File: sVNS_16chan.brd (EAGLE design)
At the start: 56.9 x 26.4 mm, 56 parts, among them IC2 OPA990IDCKR, IC3 EFM8SB10F2G-A-QFN20, J1 M50-3631042, J2 M50-3631042, J3 M50-3631042, U1 NT3H2211W0FHKH, U2 LT8410EDC-1#TRMPBF, U3 MUX36S16IRSNR, U4 MUX36S16IRSNR

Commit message: Checkpoint 5. Closer to success?
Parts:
- moved R17 7.02 mm to (2.03, 10.7)
- moved R24 4.50 mm to (12.0, 20.0), turned to 270 degrees
- moved R27 2.32 mm to (1.52, 4.88)
- moved R12 1.83 mm to (14.1, 19.2)
- moved C14 1.36 mm to (3.96, 23.7)
- moved C3 1.22 mm to (4.65, 15.8)
- moved L1 0.36 mm to (6.68, 17.2), turned to 90 degrees
- moved R26 0.20 mm to (1.12, 8.64), turned to 180 degrees
- moved R23 0.15 mm to (9.35, 21.2), turned to 180 degrees
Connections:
- net +3.3V: now also R23.1; no longer L1.P$1, R23.2, U2.2
- net +3.3V_LT8410_VCC: now also L1.P$1, R23.2, U2.2; no longer R23.1
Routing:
- net +20V: track 0.27 -> 29.0 mm, vias 0 -> 5
- net GND: track 31.6 -> 45.2 mm, vias 2 -> 13
- net +20V_PIN: track 1.63 -> 12.4 mm
- net +3.3V: track 9.32 -> 18.1 mm, vias 0 -> 4
- net +3.3V_LT8410_VCC: track 2.75 -> 10.5 mm
- net I_OUT+: track 33.5 -> 40.4 mm, vias 3 -> 5
- net MUX36D08_+20V: track 1.71 -> 7.85 mm
- net MUX36S16B_+20V: track 0.00 -> 4.85 mm
- net OPAMP_+20V: track 1.62 -> 5.43 mm
- net MUX36S16A+20V: track 0.00 -> 3.44 mm
- net RSTB_/_C2CK: track 18.1 -> 21.2 mm
- net +3.3V_VDD: track 6.31 -> 9.28 mm
- net P2.7_/_C2D: track 13.5 -> 15.4 mm
- net SW: track 1.69 -> 3.17 mm
- net P0.5_SHDN: track 36.6 -> 36.0 mm
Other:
- board text added: "Converted 20V"
- board text added: "Generated 3.3V"

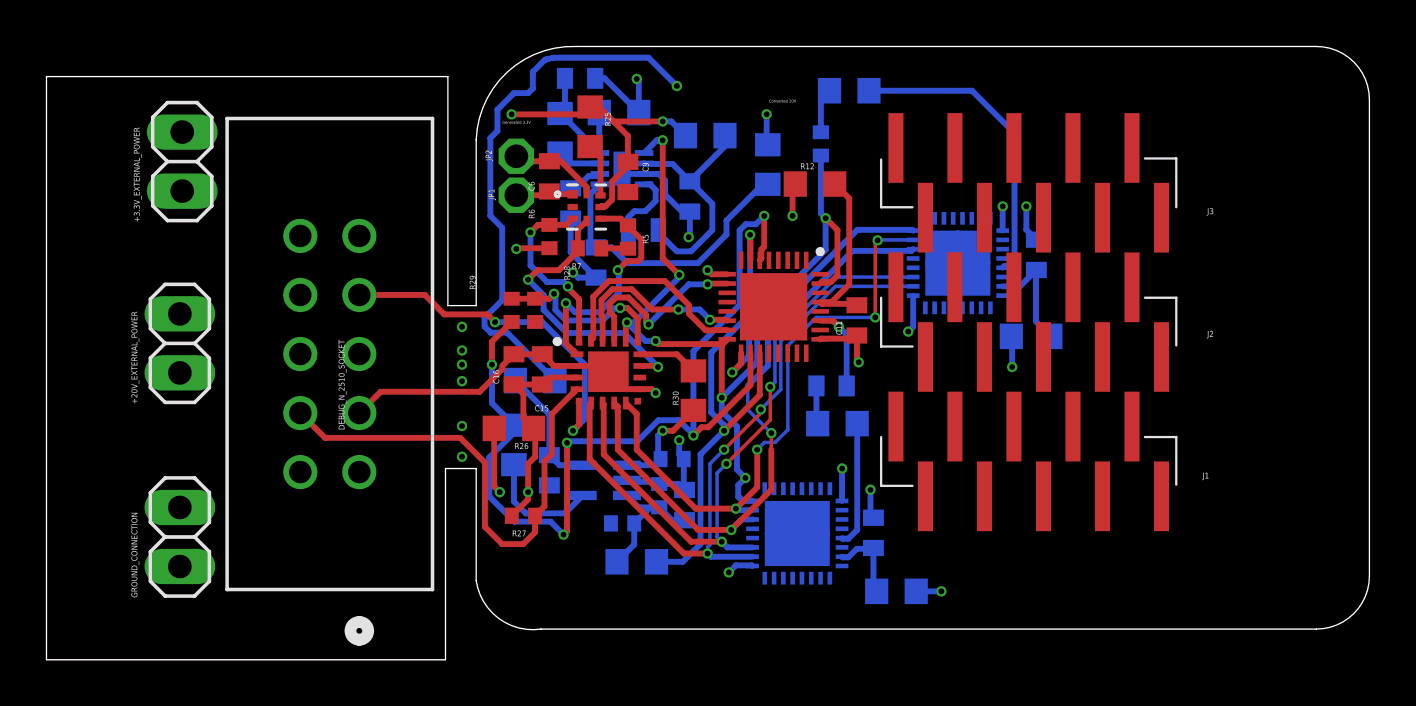
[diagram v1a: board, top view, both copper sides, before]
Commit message: Component routing finished. ready for output stage routing.
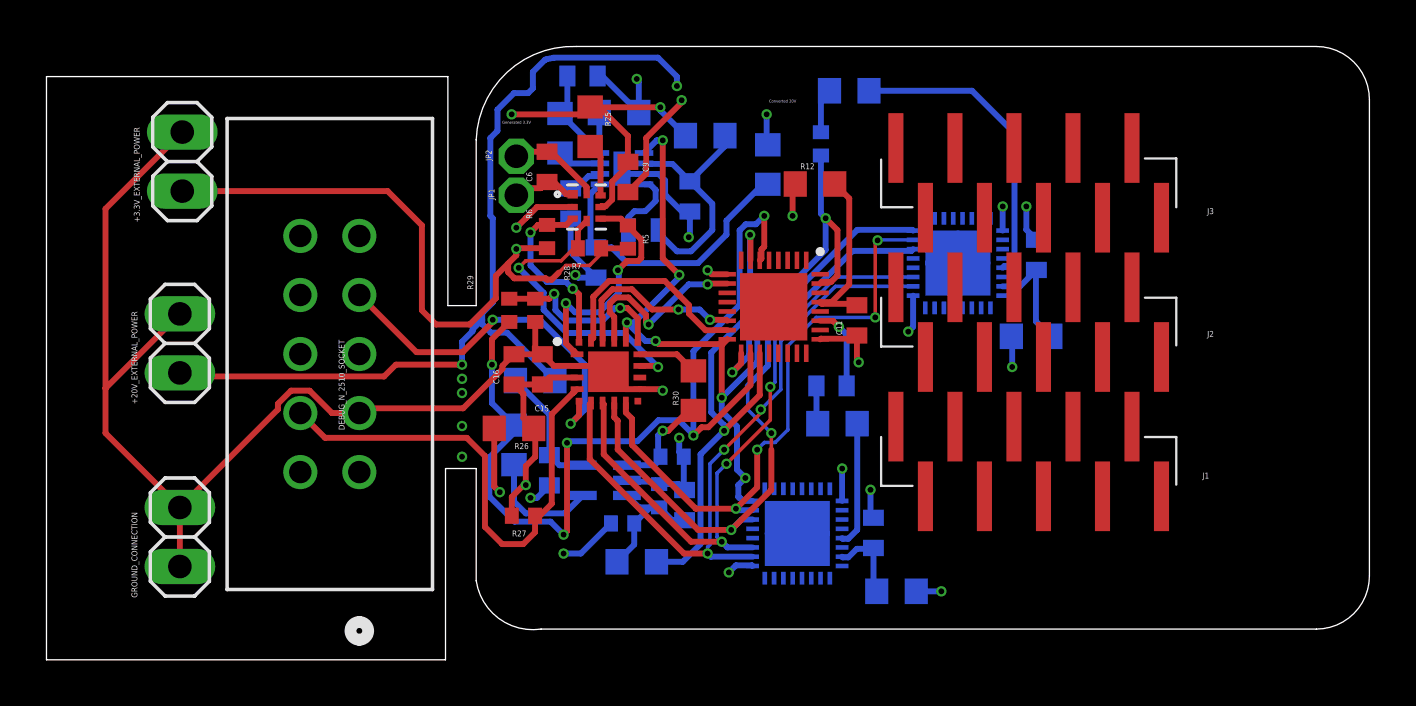
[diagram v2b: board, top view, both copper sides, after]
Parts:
- moved C6 0.42 mm to (2.54, 19.9)
- moved C14 0.14 mm to (4.06, 23.8)
- moved R9 0.10 mm to (7.92, 7.42)
- moved R29 0.10 mm to (0.91, 13.7)
- moved R6 0.10 mm to (2.54, 16.9)
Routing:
- net GND: track 45.2 -> 91.9 mm, vias 13 -> 16
- net +3.3V: track 18.1 -> 47.7 mm, vias 4 -> 5
- net +20V: track 29.0 -> 43.6 mm, vias 5 -> 6
- net P1.0_FD: track 12.4 -> 13.2 mm
- net P2.7_/_C2D: track 15.4 -> 16.1 mm

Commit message: Decreased the board size. Removed dimensions
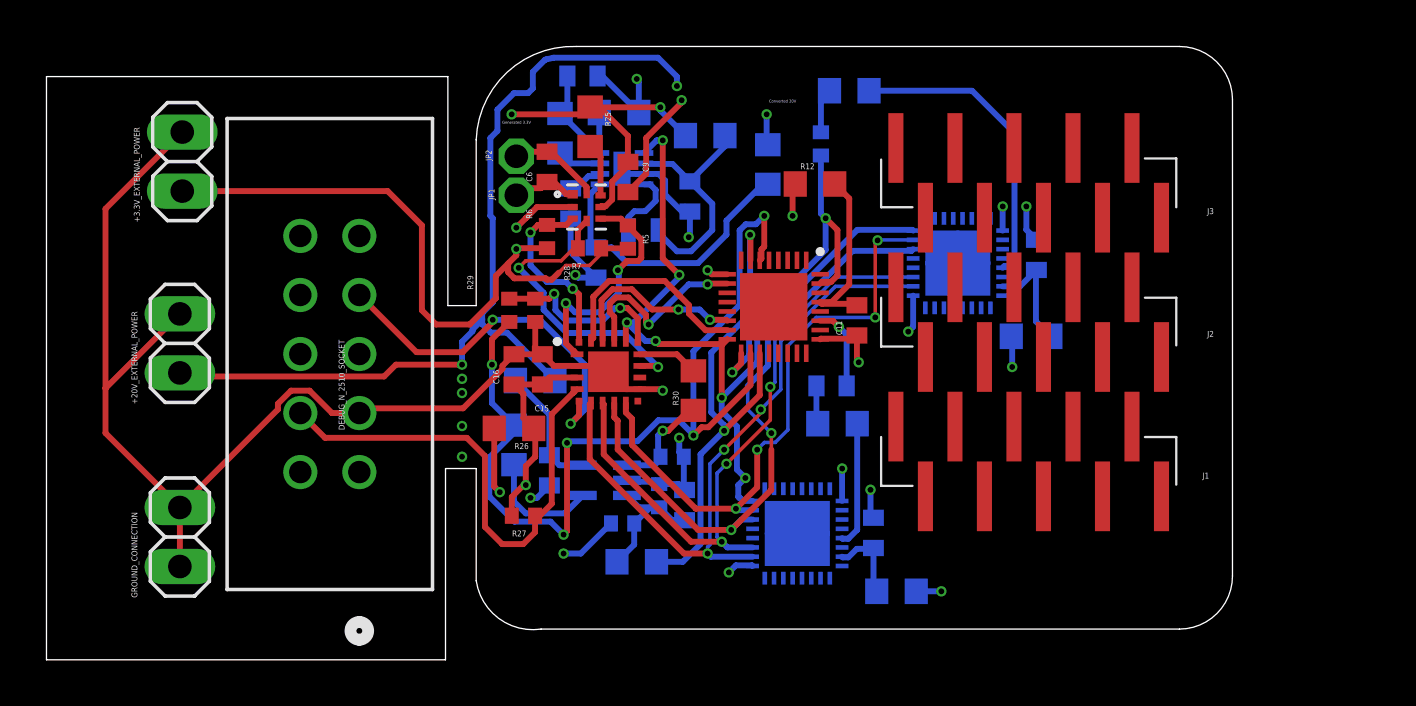
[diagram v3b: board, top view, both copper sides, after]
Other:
- board size 56.9 x 26.4 mm -> 51 x 26.4 mm
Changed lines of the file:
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@@
 <wire x1="-0.508" y1="6.9088" x2="-0.508" y2="2.0828" width="0" layer="20"/>
 <wire x1="-0.508" y1="2.0828" x2="2.286" y2="0" width="0" layer="20" curve="90"/>
-<wire x1="2.286" y1="0" x2="35.6416" y2="0" width="0" layer="20"/>
-<wire x1="35.6416" y1="0" x2="37.9276" y2="2.286" width="0" layer="20" curve="90"/>
-<wire x1="37.9276" y1="2.286" x2="37.9276" y2="22.784" width="0" layer="20"/>
-<wire x1="37.9276" y1="22.784" x2="35.6416" y2="25.07" width="0" layer="20" curve="90"/>
-<wire x1="35.6416" y1="25.07" x2="3.81" y2="25.07" width="0" layer="20"/>
+<wire x1="2.286" y1="0" x2="29.7488" y2="0" width="0" layer="20"/>
+<wire x1="29.7488" y1="0" x2="32.0348" y2="2.286" width="0" layer="20" curve="90"/>
+<wire x1="32.0348" y1="2.286" x2="32.0348" y2="22.784" width="0" layer="20"/>
+<wire x1="32.0348" y1="22.784" x2="29.7488" y2="25.07" width="0" layer="20" curve="90"/>
+<wire x1="29.7488" y1="25.07" x2="3.81" y2="25.07" width="0" layer="20"/>
 <wire x1="3.81" y1="25.07" x2="-0.508" y2="21.0568" width="0" layer="20" curve="90"/>
-<dimension x1="23.2664" y1="19.2024" x2="23.2664" y2="13.208" x3="43.7896" y3="16.2052" textsize="1.778" layer="1"/>
-<dimension x1="23.2664" y1="7.2136" x2="23.2664" y2="13.208" x3="49.276" y3="10.2108" textsize="1.778" layer="1"/>
-<dimension x1="0" y1="21.26" x2="37.8968" y2="21.336" x3="18.93616875" y3="27.395403125" textsize="1.778" layer="1"/>
-<dimension x1="35.6416" y1="0" x2="35.6416" y2="25.07" x3="56.2864" y3="12.535" textsize="1.778" layer="1"/>
-<text x="33.6296" y="22.0472" size="0.508" layer="26" font="vector">+20V
+<text x="30.2768" y="21.0312" size="0.508" layer="26" font="vector" rot="R90">+20V
 plane</text>
 <text x="2.4384" y="22.352" size="0.508" layer="26" font="vector" rot="R90">+3.3V
@@
 <polygon width="0.3048" layer="2" isolate="0.3048">
 <vertex x="3.6068" y="24.5364"/>
-<vertex x="35.3568" y="24.5364" curve="-90"/>
-<vertex x="37.338" y="22.5552"/>
-<vertex x="37.338" y="2.5908" curve="-90"/>
-<vertex x="35.052" y="0.3048"/>
+<vertex x="29.4132" y="24.5364" curve="-90"/>
+<vertex x="31.6992" y="22.2504"/>
+<vertex x="31.6992" y="2.5908" curve="-90"/>
+<vertex x="29.4132" y="0.3048"/>
 <vertex x="2.8956" y="0.3048" curve="-90"/>
 <vertex x="-0.3048" y="3.5052"/>
@@
 <wire x1="-16.4592" y1="10.3632" x2="-16.4592" y2="18.0848" width="0.254" layer="1"/>
 <wire x1="-16.4592" y1="18.0848" x2="-13.1572" y2="21.3868" width="0.254" layer="1"/>
+<wire x1="22.1488" y1="18.1864" x2="23.1648" y2="18.1864" width="0" layer="19" extent="1-1"/>
+<wire x1="18.2934" y1="14.348" x2="22.1434" y2="17.148003125" width="0" layer="19" extent="16-16"/>
+<wire x1="15.875" y1="12.6342" x2="18.0848" y2="12.8016" width="0" layer="19" extent="1-1"/>
+<wire x1="15.24" y1="6.9088" x2="15.9512" y2="11.4808" width="0" layer="19" extent="1-1"/>
+<wire x1="16.4592" y1="5.9944" x2="15.2346" y2="5.514803125" width="0" layer="19" extent="16-16"/>
+<wire x1="11.3846" y1="2.7148" x2="15.2346" y2="5.514803125" width="0" layer="19" extent="16-16"/>
+<wire x1="8.4582" y1="5.984" x2="10.3632" y2="2.4384" width="0" layer="19" extent="16-16"/>
 <wire x1="7.5184" y1="10.2616" x2="8.2296" y2="8.2296" width="0" layer="19" extent="1-1"/>
+<wire x1="3.7592" y1="15.24" x2="2.032" y2="13.216" width="0" layer="19" extent="1-1"/>
+<wire x1="3.6418" y1="18.161" x2="3.556" y2="17.6634" width="0" layer="19" extent="1-16"/>
+<wire x1="6.0198" y1="18.8064" x2="3.6418" y2="18.161" width="0" layer="19" extent="1-1"/>
+<wire x1="6.7158" y1="19.587" x2="6.223" y2="18.8064" width="0" layer="19" extent="1-16"/>
+<wire x1="9.4488" y1="15.4432" x2="8.636" y2="16.8656" width="0" layer="19" extent="1-1"/>
+<wire x1="6.4888" y1="22.225" x2="8.3312" y2="22.7584" width="0" layer="19" extent="16-16"/>
+<wire x1="2.6416" y1="6.1826" x2="5.9792" y2="6.4008" width="0" layer="19" extent="16-16"/>
 </signal>
 <signal name="I_OUT+">
@@
 <wire x1="13.2216" y1="19.1516" x2="12.954" y2="19.1516" width="0.254" layer="1"/>
 <polygon width="0.3048" layer="15" isolate="0.3048">
-<vertex x="6.096" y="24.0792"/>
-<vertex x="34.5948" y="24.0792" curve="-90"/>
-<vertex x="36.8808" y="21.7932"/>
-<vertex x="36.8808" y="2.9972" curve="-90"/>
-<vertex x="34.5948" y="0.7112"/>
-<vertex x="6.341284375" y="0.7112" curve="45"/>
+<vertex x="6.096" y="23.9776"/>
+<vertex x="28.9052" y="23.9776" curve="-90"/>
+<vertex x="31.1912" y="21.6916"/>
+<vertex x="31.1912" y="2.8956" curve="-90"/>
+<vertex x="28.9052" y="0.6096"/>
 <vertex x="6.096" y="0.6096"/>
 </polygon>

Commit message: Mapped output stage in the schematics
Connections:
- net S10A renamed S10A_11
- net S10B renamed S10B_24
- net S11A renamed S11A_20
- net S11B renamed S11B_18
- net S12A renamed S12A_25
- net S12B renamed S12B_10
- net S13A renamed S13A_30
- net S13B renamed S13B_5
- net S15A renamed S15A_2
- net S15B renamed S15B_17
- net S16A renamed S16A_1
- net S16B renamed S16B_19
- net S1A renamed S1A_14
- net S1B renamed S1B_22
- net S2A renamed S2A_8
- net S2B renamed S2B_27
- net S3A renamed S3A_3
- net S3B renamed S3B_15
- net S4A renamed S4A_13
- net S4B renamed S4B_4
- net S5A renamed S5A_26
- net S5B renamed S5B_9
- net S6A renamed S6A_21
- net S6B renamed S6B_16
- net S7A renamed S7A_12
- net S7B renamed S7B_23
- net S8A renamed S8A_7
- net S8B renamed S8B_28
- net S9A renamed S9A_6
- net S9B renamed S9B_29
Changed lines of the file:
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@@
 <wire x1="6.2992" y1="17.9832" x2="6.7718" y2="17.9832" width="0.254" layer="16"/>
 </signal>
-<signal name="S16A">
+<signal name="S16A_1">
 <contactref element="U3" pad="1"/>
 </signal>
-<signal name="S15A">
+<signal name="S15A_2">
 <contactref element="U3" pad="2"/>
 </signal>
@@
 <contactref element="U3" pad="3"/>
 </signal>
-<signal name="S13A">
+<signal name="S13A_30">
 <contactref element="U3" pad="4"/>
 </signal>
-<signal name="S12A">
+<signal name="S12A_25">
 <contactref element="U3" pad="5"/>
 </signal>
-<signal name="S11A">
+<signal name="S11A_20">
 <contactref element="U3" pad="6"/>
 </signal>
-<signal name="S10A">
+<signal name="S10A_11">
 <contactref element="U3" pad="7"/>
 </signal>
-<signal name="S9A">
+<signal name="S9A_6">
 <contactref element="U3" pad="8"/>
 </signal>
-<signal name="S8A">
+<signal name="S8A_7">
 <contactref element="U3" pad="24"/>
 </signal>
-<signal name="S7A">
+<signal name="S7A_12">
 <contactref element="U3" pad="23"/>
 </signal>
-<signal name="S6A">
+<signal name="S6A_21">
 <contactref element="U3" pad="22"/>
 </signal>
-<signal name="S5A">
+<signal name="S5A_26">
 <contactref element="U3" pad="21"/>
 </signal>
-<signal name="S4A">
+<signal name="S4A_13">
 <contactref element="U3" pad="20"/>
 </signal>
-<signal name="S3A">
+<signal name="S3A_3">
 <contactref element="U3" pad="19"/>
 </signal>
-<signal name="S2A">
+<signal name="S2A_8">
 <contactref element="U3" pad="18"/>
 </signal>
-<signal name="S1A">
+<signal name="S1A_14">
 <contactref element="U3" pad="17"/>
 </signal>
@@
 <wire x1="11.2332" y1="13.02021875" x2="14.5288" y2="16.31581875" width="0.254" layer="16"/>
 </signal>
-<signal name="S16B">
+<signal name="S16B_19">
 <contactref element="U4" pad="1"/>
 </signal>
-<signal name="S15B">
+<signal name="S15B_17">
 <contactref element="U4" pad="2"/>
 </signal>
@@
 <contactref element="U4" pad="3"/>
 </signal>
-<signal name="S13B">
+<signal name="S13B_5">
 <contactref element="U4" pad="4"/>
 </signal>
-<signal name="S12B">
+<signal name="S12B_10">
 <contactref element="U4" pad="5"/>
 </signal>
-<signal name="S11B">
+<signal name="S11B_18">
 <contactref element="U4" pad="6"/>
 </signal>
-<signal name="S10B">
+<signal name="S10B_24">
 <contactref element="U4" pad="7"/>
 </signal>
-<signal name="S9B">
+<signal name="S9B_29">
 <contactref element="U4" pad="8"/>
 </signal>
-<signal name="S8B">
+<signal name="S8B_28">
 <contactref element="U4" pad="24"/>
 </signal>
-<signal name="S7B">
+<signal name="S7B_23">
 <contactref element="U4" pad="23"/>
 </signal>
-<signal name="S6B">
+<signal name="S6B_16">
 <contactref element="U4" pad="22"/>
 </signal>
-<signal name="S5B">
+<signal name="S5B_9">
 <contactref element="U4" pad="21"/>
 </signal>
-<signal name="S4B">
+<signal name="S4B_4">
 <contactref element="U4" pad="20"/>
 </signal>
-<signal name="S3B">
+<signal name="S3B_15">
 <contactref element="U4" pad="19"/>
 </signal>
-<signal name="S2B">
+<signal name="S2B_27">
 <contactref element="U4" pad="18"/>
 </signal>
-<signal name="S1B">
+<signal name="S1B_22">
 <contactref element="U4" pad="17"/>
 </signal>

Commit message: Signal tracing. Checkpoint 1
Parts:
- IC3: value EFM8SB10F2G-A-QFN20 -> EFM8SB10F8A-A-QFN24EFM8SB10F8A-A-QFN24; device SamacSys_Parts:EFM8SB10F8GAQFN20R -> sVNS_16chan_lib:QFN50P400X400X80-25T245N
- moved R27 11.1 mm to (-8.53, 0.20), turned to 0 degrees
- moved R30 1.64 mm to (10.3, 9.45), turned to 180 degrees
- moved R26 1.22 mm to (2.34, 8.53), turned to 0 degrees
- moved C16 1.22 mm to (2.03, 12.0)
- moved R12 1.12 mm to (14.2, 20.3)
- moved C15 1.08 mm to (3.05, 12.0)
- moved IC3 0.87 mm to (5.99, 11.4)
- moved R28 0.72 mm to (1.93, 14.4)
- moved R29 0.72 mm to (0.81, 14.4)
- moved C10 0.10 mm to (16.7, 4.14)
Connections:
- net P1.5_MUXS16_A1 renamed P1.6_MUXS16_A1
- removed net P1.1: IC3.13
- removed net P1.2: IC3.11
- removed net P1.3_MUXS16_A0: IC3.10, U3.15, U4.15
- removed net P1.6_MUXS16_A2: IC3.8, U3.11, U4.11
- removed net P1.7_MUXS16_A3: IC3.7, U3.10, U4.10
- new net P1.4_MUXS16_A3: IC3.12, U3.10, U4.10
- new net P1.5_MUXS16_A2: IC3.11, U3.11, U4.11
- new net P1.7_MUXS16_A0: IC3.8, U3.15, U4.15
- net +3.3V_VDD: now also IC3.3; no longer IC3.4
- net GND: now also IC3.2, IC3.25; no longer IC3.12, IC3.21, IC3.3
- net P0.0_SMBUS0_SDA: now also IC3.24; no longer IC3.2
- net P0.1_SMBUS0_SCL: now also IC3.23; no longer IC3.1
- net P0.2_MUXD08_A0: now also IC3.22; no longer IC3.20
- net P0.3_MUXD08_A1: now also IC3.21; no longer IC3.19
- net P0.4_MUXD08_A2: now also IC3.20; no longer IC3.18
- net P0.5_SHDN: now also IC3.19; no longer IC3.17
- net P0.6_ADC: now also IC3.18; no longer IC3.16
- net P0.7_IREF_PIN: now also IC3.17; no longer IC3.15
- net P1.0_FD: now also IC3.16; no longer IC3.14
- net P2.7_/_C2D: now also IC3.7; no longer IC3.6
- net RSTB_/_C2CK: now also IC3.6; no longer IC3.5
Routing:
- net GND: track 91.9 -> 28.7 mm, vias 16 -> 15
- net +3.3V: track 47.7 -> 8.66 mm, vias 5 -> 1
- net +20V: track 43.6 -> 8.32 mm, vias 6 -> 3
- net I_OUT+: track 40.4 -> 7.84 mm, vias 5 -> 3
- net P0.5_SHDN: track 36.0 -> 4.56 mm, vias 6 -> 4
- net P1.7_MUXS16_A3: track 28.3 -> 0.00 mm, vias 3 -> 0
- net P1.6_MUXS16_A2: track 27.2 -> 0.00 mm, vias 3 -> 0
- net P1.3_MUXS16_A0: track 25.6 -> 0.00 mm, vias 4 -> 0
- net P1.6_MUXS16_A1: track 27.1 -> 3.59 mm, vias 2 -> 3
- net RSTB_/_C2CK: track 21.5 -> 1.11 mm, vias 0 -> 1
- net I_OUT-: track 21.9 -> 2.31 mm
- net P2.7_/_C2D: track 16.1 -> 0.88 mm, vias 2 -> 1
- net P1.0_FD: track 13.2 -> 3.62 mm
- net P0.0_SMBUS0_SDA: track 10.3 -> 2.16 mm, vias 2 -> 1
- net DB: track 15.6 -> 7.62 mm, vias 2 -> 3
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
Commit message: Signal tracing. Checkpoint 2
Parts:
- moved R28 12.5 mm to (11.8, 6.81)
- moved R29 12.5 mm to (10.7, 6.81)
- moved R19 11.5 mm to (26.3, 9.04), turned to 270 degrees
- moved R15 10.3 mm to (24.8, 12.3)
- moved C10 8.96 mm to (24.2, 9.02)
- moved U3 8.96 mm to (20.8, 8.99)
- moved R20 7.20 mm to (22.3, 19.7), turned to 270 degrees
- moved R13 6.12 mm to (17.3, 15.5), turned to 180 degrees
- moved R14 5.59 mm to (21.1, 23.1), turned to 180 degrees
- moved IC3 5.38 mm to (5.99, 5.99)
- moved C4 5.38 mm to (19.8, 12.5), turned to 180 degrees
- moved C16 5.10 mm to (1.63, 6.91)
- moved C15 5.09 mm to (2.74, 6.91)
- moved C5 4.68 mm to (20.5, 19.7)
- moved U4 4.68 mm to (17.2, 19.3)
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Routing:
- net P1.7_MUXS16_A0: track 4.01 -> 98.2 mm, vias 3 -> 2
- net P1.6_MUXS16_A1: track 3.59 -> 88.5 mm, vias 3 -> 2
- net P1.5_MUXS16_A2: track 3.50 -> 81.4 mm, vias 3 -> 2
- net P1.4_MUXS16_A3: track 6.32 -> 79.8 mm, vias 3 -> 2
- net P1.0_FD: track 3.62 -> 35.6 mm
- net P0.5_SHDN: track 4.56 -> 36.1 mm
- net RSTB_/_C2CK: track 1.11 -> 28.4 mm, vias 1 -> 0
- net P2.7_/_C2D: track 0.88 -> 22.8 mm, vias 1 -> 0
- net GND: track 28.7 -> 41.0 mm, vias 15 -> 18
- net BAL_B_PIN: track 1.94 -> 12.6 mm
- net P0.1_SMBUS0_SCL: track 2.02 -> 12.5 mm, vias 1 -> 2
- net P0.0_SMBUS0_SDA: track 2.16 -> 11.9 mm, vias 1 -> 2
- net BAL_B: track 13.6 -> 4.62 mm
- net P0.4_MUXD08_A2: track 1.53 -> 10.1 mm, vias 1 -> 2
- net +20V: track 8.32 -> 0.00 mm, vias 3 -> 0
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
